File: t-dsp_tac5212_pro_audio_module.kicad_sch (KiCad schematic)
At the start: 119 parts, among them T108 Tab, T109 Tab, T110 Tab, T111 Tab, U108 Single Buffer with Tri-state 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, U109 3.3v LDO - TLV74133PDBVR

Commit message: fix all drc errors.
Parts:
- 3V108, 5V108, DOUT108, E108, E109, G117, G118, G119, GND108, MCLK108, NT108, NT109, PU_EN108, SCL108, SDA108: symbol Device:NetTie_2 -> proejct_lib:NetTie_2
- ADD108: symbol proejct_lib:Jumper_NO_Small-Device_2 -> project_lib_tac5212:Jumper_NO_Small-Device_2
- ADD110, ADD111: symbol Device:NetTie_2 -> project_lib_tac5212:Jumper_NO_Small-Device_2
- ADD112: symbol proejct_lib:Jumper_NO_Small-Device_1 -> project_lib_tac5212:Jumper_NO_Small-Device_1
- C124, C125, C126, C127: symbol proejct_lib:C_Polarized_Small -> proejct_lib:C_Small
- D108, D109, D110, D111, D112, D113, D114, D115: symbol proejct_lib:SP0502BAJT_2 -> proejct_lib:TPD1E10B06
- FB108, FB109, FB110, FB111: footprint project_fp:C_0805_2012Metric_Pad1.18x1.45mm_HandSolder -> project_fp:L_0805_2012Metric_Pad1.18x1.45mm_HandSolder
- R108, R109, R111, R116, R127, R129, R130, R131, R132, R133, R134, R135, R136, R137, R138, R139: footprint Capacitor_SMD:C_0603_1608Metric_Pad1.08x0.95mm_HandSolder -> project_fp:R_0603_1608Metric_Pad1.05x0.95mm_HandSolder
- R128: footprint project_fp:R_0402_1005Metric -> project_fp:R_0805_2012Metric_Pad1.20x1.40mm_HandSolder; Digikey (none) -> ERJ-3EKF1000V; Manufacturer (none) -> Bourns; Manufacturer_Part_Number (none) -> CMP0805AFX-1000ELF; Package / Case R0402 -> R0805; mouser (none) -> 652-CMP0805AFX-1000L; now left out of the parts list
- SCL109: footprint Resistor_SMD:R_0402_1005Metric_Pad0.72x0.64mm_HandSolder -> project_fp:jumper_slice_1mm; symbol Device:NetTie_2 -> proejct_lib:NetTie_2; Label SC -> 3V
- board_outline108: symbol proejct_lib:Conn_02x33_Odd_Even -> proejct_lib:t-dsp_expansion_connector; now in the parts list
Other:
- moved on the sheet: 5V108

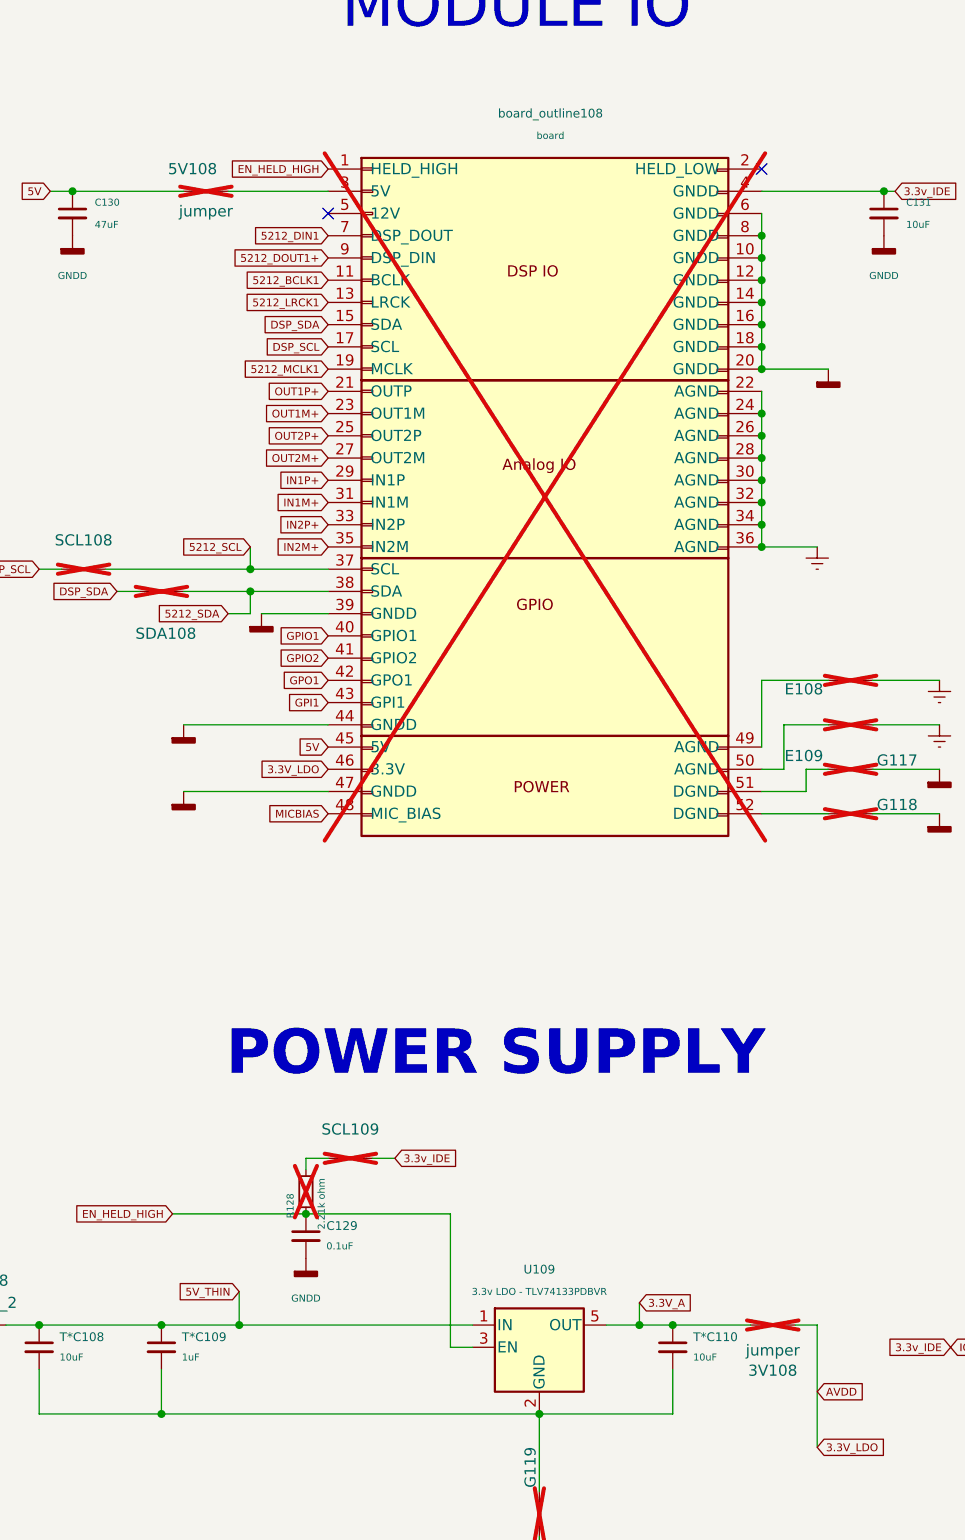
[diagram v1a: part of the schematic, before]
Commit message: Add KiBot CI/CD pipeline for JLCPCB manufacturing files
- Add .kibot.yaml config for gerbers, drill, BOM, CPL, and ZIP output
- Add GitHub Actions workflow triggered on push to main and manual dispatch
- Add release job to attach JLCPCB ZIP to GitHub Releases on version tags
- Fix malformed reference designators (5V108, 3V108) that blocked KiBot BOM/CPL
- Add local build instructions to README
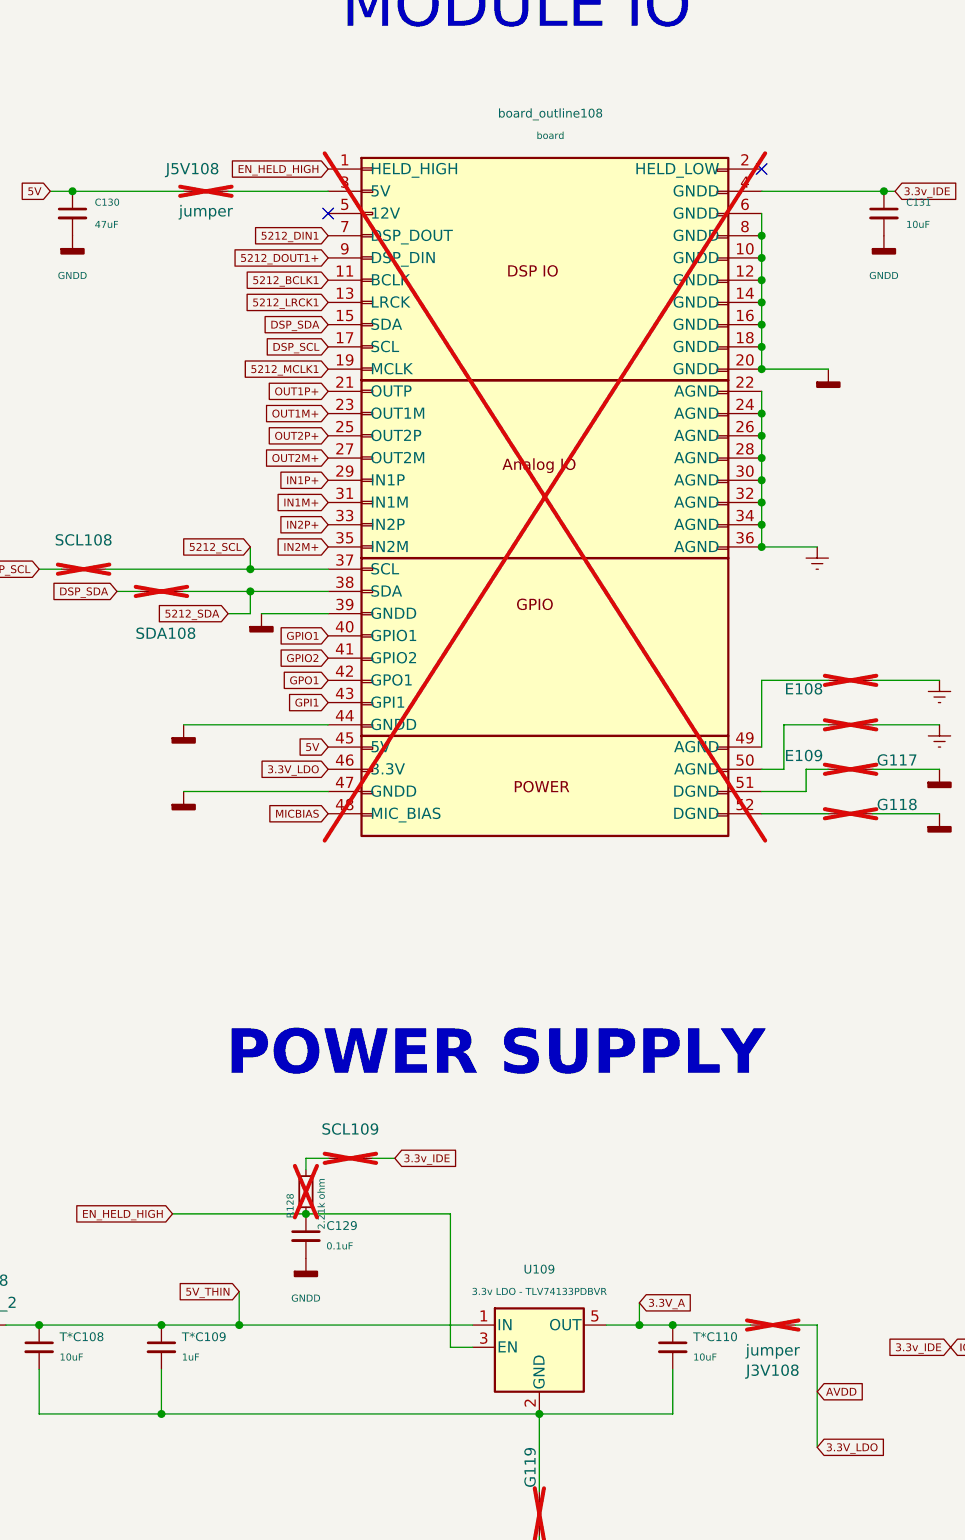
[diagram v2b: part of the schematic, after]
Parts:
- renumbered 3V108 to J3V108, 5V108 to J5V108
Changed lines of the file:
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@@
 		(on_board yes)
 		(dnp yes)
-		(property "Reference" "5V108"
+		(property "Reference" "J5V108"
 			(at 50.546 223.52 0)
 			(effects
@@
 			(project "tac5212_audio_board_single_ended"
 				(path "/8cee3af6-3893-45a9-89a4-21657973eeff"
-					(reference "5V108")
+					(reference "J5V108")
 					(unit 1)
 				)
@@
 		(on_board yes)
 		(dnp yes)
-		(property "Reference" "3V108"
+		(property "Reference" "J3V108"
 			(at 116.84 360.807 0)
 			(effects
@@
 			(project "tac5212_audio_board_single_ended"
 				(path "/8cee3af6-3893-45a9-89a4-21657973eeff"
-					(reference "3V108")
+					(reference "J3V108")
 					(unit 1)
 				)
